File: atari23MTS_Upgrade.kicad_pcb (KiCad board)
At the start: 2 copper layers, 136 x 88 mm, 58 parts, among them P1 CONN_01X01, P2 CONN_01X01, P3 CONN_01X01, P4 CONN_01X01, P5 CONN_01X01, P6 CONN_01X01, SW1 SW_PUSH, U1 NCP1117ST33T3G, U10 TXB0108-PW, U11 ISSI61WV5128BL, U12 ISSI61WV5128BL, U13 ISSI61WV5128BL, U14 ISSI61WV5128BL, U2 STM32F401RCTx, U3 74LS138, U4 TXB0108-PW, U5 TXB0108-PW, U6 TXB0108-PW, U7 74HC04, U8 TXB0108-PW, U9 74LS32

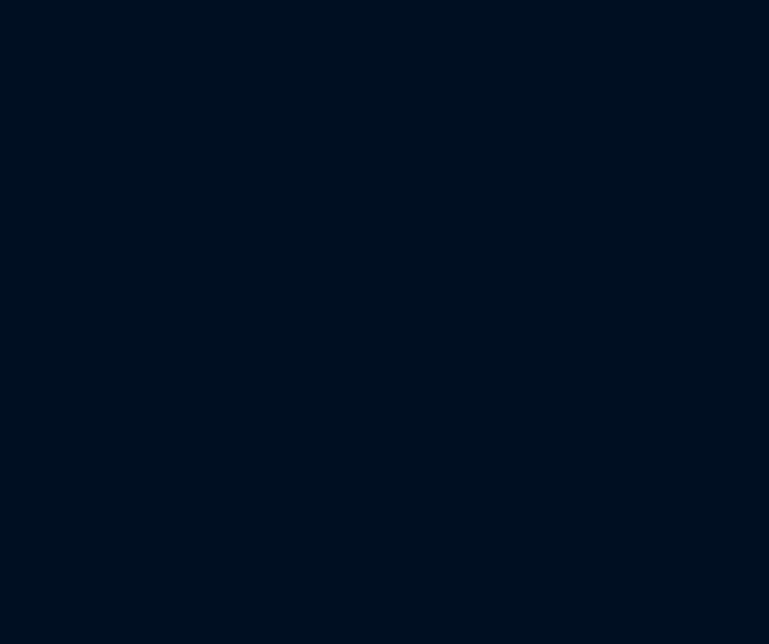
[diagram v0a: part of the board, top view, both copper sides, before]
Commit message: Modified silkscreen
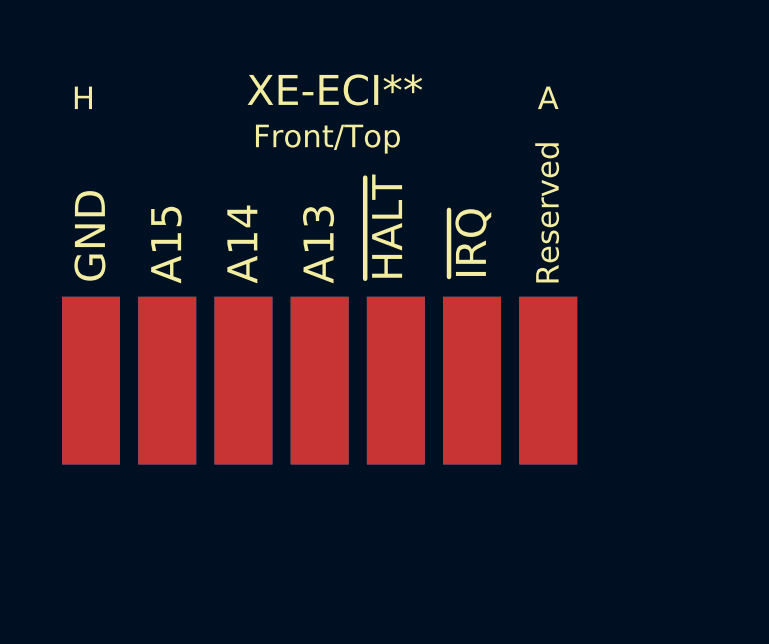
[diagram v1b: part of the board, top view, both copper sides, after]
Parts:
- removed LOGO: LOGO, RetroBitLab:atari_fuji_SilkScreen_21.2x25-RevBack
- added G***: LOGO, RetroBitLab:atari_fuji_SilkScreen_21.2x25-Rev, B.Cu at (152.4, 86.4)
- added XE-ECI**: ATARI-XE-ECI-SLOT, ATARI-XE-ECI-SLOT, F.Cu at (0.00, 0.00)

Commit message: Updated after footprint ECI Change
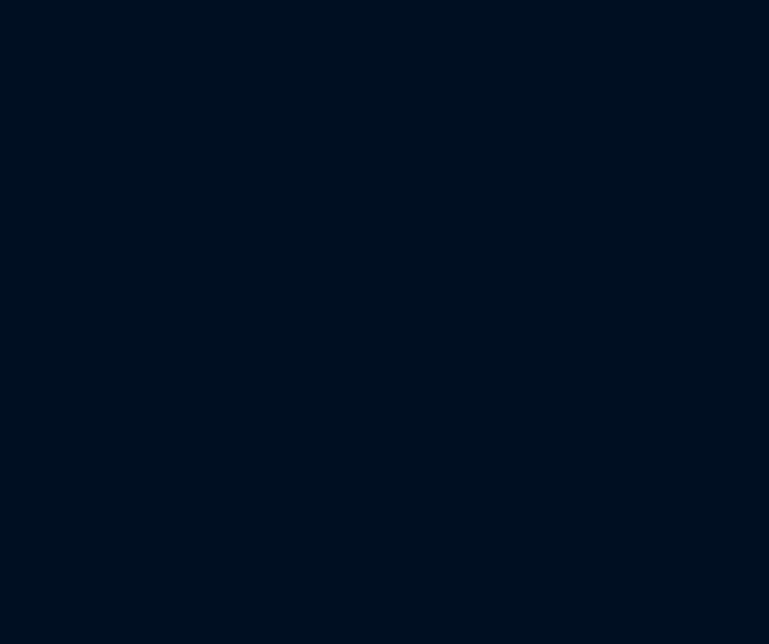
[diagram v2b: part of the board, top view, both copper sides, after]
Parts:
- removed XE-ECI**: ATARI-XE-ECI-SLOT, ATARI-XE-ECI-SLOT
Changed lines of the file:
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@@
 (kicad_pcb (version 4) (host pcbnew 4.0.2+dfsg1-stable)
   (general
-    (links 0)
+    (links 356)
     (no_connects 0)
-    (area 84.949999 50.449999 221.050001 138.550001)
+    (area -0.45 -14.587 243.5 161.200001)
     (thickness 1.6)
     (drawings 48)
     (tracks 2906)
     (zones 0)
-    (modules 59)
+    (modules 58)
     (nets 108)
   )
@@
     (uvia_drill 0.1)
   )
-  (module ATARI-XE-ECI-SLOT (layer F.Cu)
-    (at 0 0)
-    (fp_text reference XE-ECI** (at 10.16 -13.462) (layer F.SilkS)
-      (effects (font (size 1 1) (thickness 0.15)))
-    )
-    (fp_text value ATARI-XE-ECI-SLOT (at 9.652 -11.938) (layer F.Fab)
-      (effects (font (size 1 1) (thickness 0.15)))
-    )
-    (fp_text user 7 (at 1.778 -13.208) (layer B.SilkS)
-      (effects (font (size 0.75 0.75) (thickness 0.15)) (justify mirror))
-    )
-    (fp_text user 1 (at 17.272 -13.208) (layer B.SilkS)
-      (effects (font (size 0.75 0.75) (thickness 0.15)) (justify mirror))
-    )
-    (fp_text user Back/Bottom (at 9.652 -12.446) (layer B.SilkS)
-      (effects (font (size 0.75 0.75) (thickness 0.15)) (justify mirror))
-    )
-    (fp_text user Front/Top (at 9.906 -11.938) (layer F.SilkS)
-      (effects (font (size 0.75 0.75) (thickness 0.15)))
-    )
-    (fp_text user H (at 1.778 -13.208) (layer F.SilkS)
-      (effects (font (size 0.75 0.75) (thickness 0.15)))
-    )
-    (fp_text user A (at 17.272 -13.208) (layer F.SilkS)
-      (effects (font (size 0.75 0.75) (thickness 0.15)))
-    )
-    (fp_text user Reserved (at 17.272 -9.398 90) (layer F.SilkS)
-      (effects (font (size 0.75 0.75) (thickness 0.15)))
-    )
-    (fp_text user ~IRQ (at 14.732 -8.382 90) (layer F.SilkS)
-      (effects (font (size 1 1) (thickness 0.15)))
-    )
-    (fp_text user ~HALT (at 11.938 -8.89 90) (layer F.SilkS)
-      (effects (font (size 1 1) (thickness 0.15)))
-    )
-    (fp_text user A13 (at 9.652 -8.382 90) (layer F.SilkS)
-      (effects (font (size 1 1) (thickness 0.15)))
-    )
-    (fp_text user A14 (at 7.112 -8.382 90) (layer F.SilkS)
-      (effects (font (size 1 1) (thickness 0.15)))
-    )
-    (fp_text user A15 (at 4.572 -8.382 90) (layer F.SilkS)
-      (effects (font (size 1 1) (thickness 0.15)))
-    )
-    (fp_text user ~REF (at 4.572 -8.636 90) (layer B.SilkS)
-      (effects (font (size 1 1) (thickness 0.15)) (justify mirror))
-    )
-    (fp_text user AUDIO (at 7.112 -9.144 90) (layer B.SilkS)
-      (effects (font (size 1 1) (thickness 0.15)) (justify mirror))
-    )
-    (fp_text user ~MPD (at 9.652 -8.636 90) (layer B.SilkS)
-      (effects (font (size 1 1) (thickness 0.15)) (justify mirror))
-    )
-    (fp_text user ~D1XX (at 12.192 -8.89 90) (layer B.SilkS)
-      (effects (font (size 1 1) (thickness 0.15)) (justify mirror))
-    )
-    (fp_text user ~RST (at 14.732 -8.382 90) (layer B.SilkS)
-      (effects (font (size 1 1) (thickness 0.15)) (justify mirror))
-    )
-    (fp_text user ~EXSEL (at 17.272 -9.144 90) (layer B.SilkS)
-      (effects (font (size 1 1) (thickness 0.15)) (justify mirror))
-    )
-    (fp_text user 5V (at 2.032 -8.128 90) (layer B.SilkS)
-      (effects (font (size 1 1) (thickness 0.15)) (justify mirror))
-    )
-    (fp_text user GND (at 2.032 -8.636 90) (layer F.SilkS)
-      (effects (font (size 1 1) (thickness 0.15)))
-    )
-    (pad A smd rect (at 17.272 -3.81 270) (size 5.588 1.9304) (layers F.Cu F.Paste F.Mask))
-    (pad 1 smd rect (at 17.272 -3.81 270) (size 5.588 1.9304) (layers B.Cu B.Paste B.Mask))
-    (pad 2 smd rect (at 14.732 -3.81 270) (size 5.588 1.9304) (layers B.Cu B.Paste B.Mask))
-    (pad 3 smd rect (at 12.192 -3.81 270) (size 5.588 1.9304) (layers B.Cu B.Paste B.Mask))
-    (pad 4 smd rect (at 9.652 -3.81 270) (size 5.588 1.9304) (layers B.Cu B.Paste B.Mask))
-    (pad 5 smd rect (at 7.112 -3.81 270) (size 5.588 1.9304) (layers B.Cu B.Paste B.Mask))
-    (pad 6 smd rect (at 4.572 -3.81 270) (size 5.588 1.9304) (layers B.Cu B.Paste B.Mask))
-    (pad 7 smd rect (at 2.032 -3.81 270) (size 5.588 1.9304) (layers B.Cu B.Paste B.Mask))
-    (pad B smd rect (at 14.732 -3.81 270) (size 5.588 1.9304) (layers F.Cu F.Paste F.Mask))
-    (pad C smd rect (at 12.192 -3.81 270) (size 5.588 1.9304) (layers F.Cu F.Paste F.Mask))
-    (pad D smd rect (at 9.652 -3.81 270) (size 5.588 1.9304) (layers F.Cu F.Paste))
-    (pad E smd rect (at 7.112 -3.81 270) (size 5.588 1.9304) (layers F.Cu F.Paste F.Mask))
-    (pad F smd rect (at 4.572 -3.81 270) (size 5.588 1.9304) (layers F.Cu F.Paste F.Mask))
-    (pad H smd rect (at 2.032 -3.81 270) (size 5.588 1.9304) (layers F.Cu F.Paste F.Mask))
-  )
   (module ATARI-LEFT-CARTRIDGE locked (layer F.Cu)
     (at 148.082 126.238)
@@
     (pad C smd rect (at 12.192 -3.81 270) (size 5.588 1.9304) (layers F.Cu F.Paste F.Mask)
       (net 40 ~HALT))
-    (pad D smd rect (at 9.652 -3.81 270) (size 5.588 1.9304) (layers F.Cu F.Paste)
+    (pad D smd rect (at 9.652 -3.81 270) (size 5.588 1.9304) (layers F.Cu F.Paste F.Mask)
       (net 41 A13))
     (pad E smd rect (at 7.112 -3.81 270) (size 5.588 1.9304) (layers F.Cu F.Paste F.Mask)

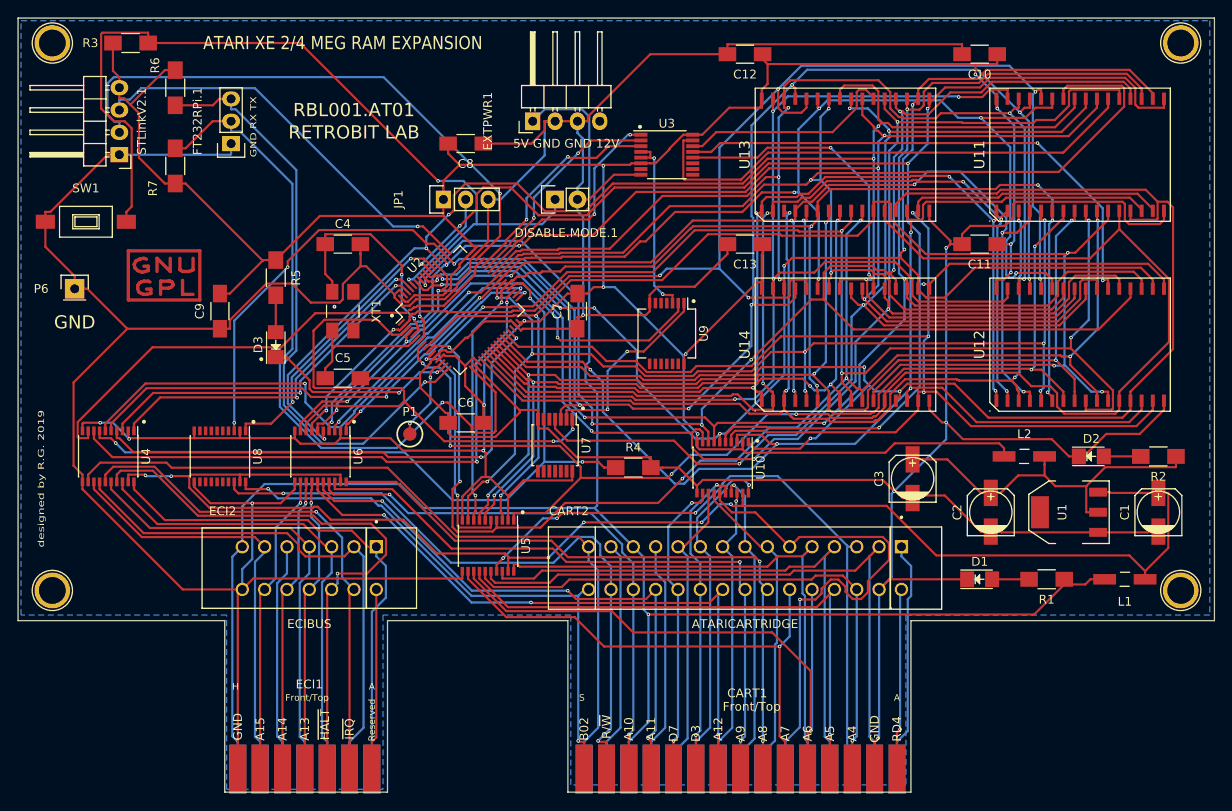
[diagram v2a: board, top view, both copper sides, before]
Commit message: Added D3xx selection logic for PIA (6520) if needed
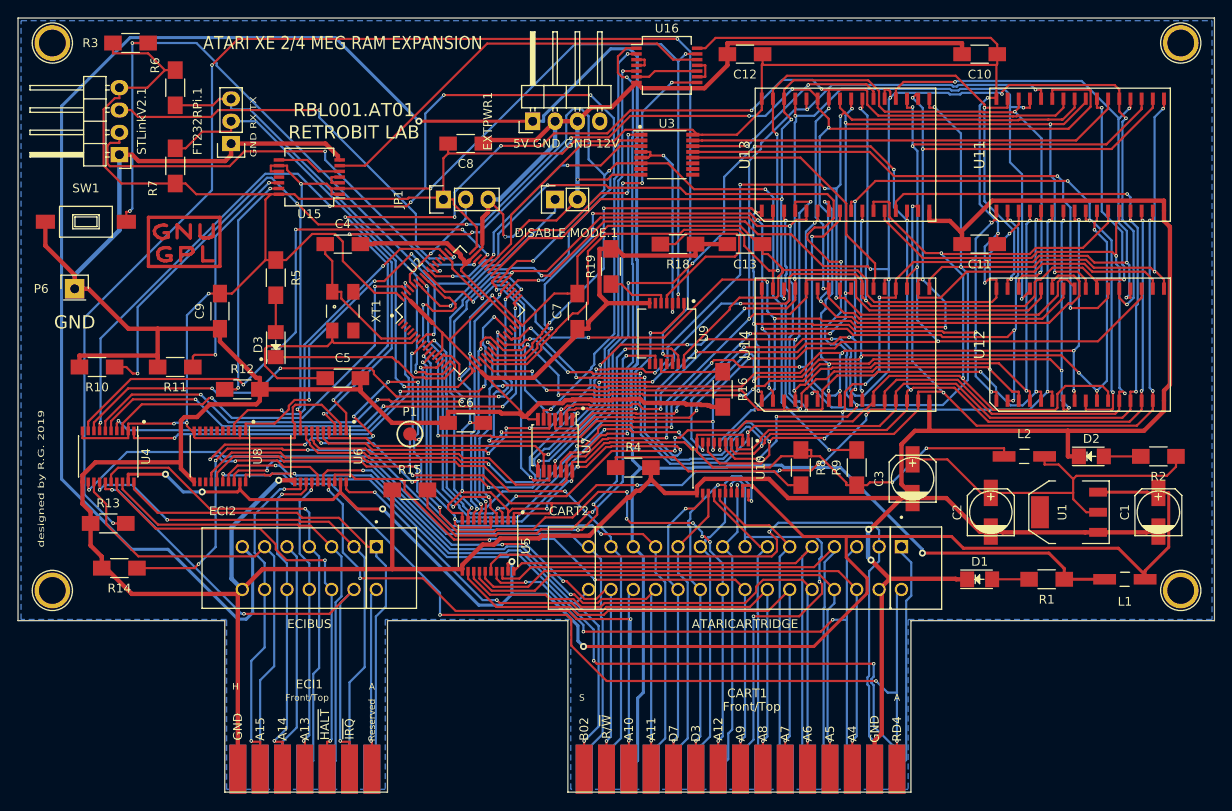
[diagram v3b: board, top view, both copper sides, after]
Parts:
- added R10: 2.2k, Resistors_SMD:R_1206_HandSoldering, F.Cu at (94.0, 90.2)
- added R11: 0, Resistors_SMD:R_1206_HandSoldering, F.Cu at (102.9, 90.2)
- added R12: 0, Resistors_SMD:R_1206_HandSoldering, F.Cu at (110.5, 92.7)
- added R13: 0, Resistors_SMD:R_1206_HandSoldering, F.Cu at (95.2, 108.0)
- added R14: 0, Resistors_SMD:R_1206_HandSoldering, F.Cu at (96.5, 113.0)
- added R15: 0, Resistors_SMD:R_1206_HandSoldering, F.Cu at (129.5, 104.1)
- added R16: 0, Resistors_SMD:R_1206_HandSoldering, F.Cu at (165.1, 92.7)
- added R18: 0, Resistors_SMD:R_1206_HandSoldering, F.Cu at (160.0, 76.2)
- added R19: 0, Resistors_SMD:R_1206_HandSoldering, F.Cu at (152.4, 78.7)
- added R8: 10K, Resistors_SMD:R_1206_HandSoldering, F.Cu at (174.0, 101.6)
- added R9: 10K, Resistors_SMD:R_1206_HandSoldering, F.Cu at (180.3, 101.6)
- added U15: 74LS08, Housings_SSOP:SSOP-14_5.3x6.2mm_Pitch0.65mm, F.Cu at (118.1, 68.6)
- added U16: 74LS08, Housings_SSOP:SSOP-14_5.3x6.2mm_Pitch0.65mm, F.Cu at (158.8, 55.9)
- moved REF** 4.44 mm to (103.9, 76.2)
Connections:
- EXTPWR1 pad 4: (no net) -> Net-(EXTPWR1-Pad4)
- P2 pad 1: (no net) -> Net-(P2-Pad1)
- P3 pad 1: (no net) -> Net-(P3-Pad1)
- P4 pad 1: (no net) -> Net-(P4-Pad1)
- P5 pad 1: (no net) -> Net-(P5-Pad1)
- R4 pad 1: ~mRST -> Net-(R4-Pad1)
- U2 pad 1: (no net) -> Net-(U2-Pad1)
- U2 pad 2: mA13 -> Net-(U2-Pad2)
- U2 pad 3: mA14 -> Net-(U2-Pad3)
- U2 pad 30: (no net) -> Net-(U2-Pad30)
- U2 pad 39: mA8 -> RAMEN
- U2 pad 4: mA15 -> Net-(U2-Pad4)
- U2 pad 40: mA9 -> ~mD3XX
- U2 pad 51: mA10 -> Net-(U2-Pad51)
- U2 pad 52: mA11 -> Net-(U2-Pad52)
- U2 pad 53: mA12 -> Net-(U2-Pad53)
- U3 pad 10: (no net) -> Net-(U3-Pad10)
- U3 pad 11: (no net) -> Net-(U3-Pad11)
- U3 pad 6: VCC3V3 -> RAMEN
- U3 pad 7: (no net) -> Net-(U3-Pad7)
- U3 pad 9: (no net) -> Net-(U3-Pad9)
- U7 pad 10: (no net) -> ~mD3XX
- U7 pad 11: (no net) -> mD3XX
- U7 pad 12: (no net) -> ~mA13
- U7 pad 13: (no net) -> mA13
- U7 pad 5: (no net) -> mA11
- U7 pad 6: (no net) -> ~mA11
- U7 pad 8: (no net) -> ~mA10
- U7 pad 9: (no net) -> mA10
- U8 pad 12: (no net) -> Net-(U8-Pad12)
- U8 pad 13: (no net) -> Net-(U8-Pad13)
- U8 pad 14: (no net) -> RD5
- U8 pad 15: (no net) -> ~S5
- U8 pad 16: (no net) -> RD4
- U8 pad 17: (no net) -> ~S4
- U8 pad 4: (no net) -> ~mS4
- U8 pad 5: (no net) -> mRD4
- U8 pad 6: (no net) -> ~mS5
- U8 pad 7: (no net) -> mRD5
- U8 pad 8: (no net) -> Net-(U8-Pad8)
- U8 pad 9: (no net) -> Net-(U8-Pad9)
- U9 pad 10: (no net) -> Net-(R16-Pad1)
- U9 pad 11: (no net) -> Net-(U9-Pad11)
- U9 pad 12: (no net) -> Net-(R13-Pad2)
- U9 pad 13: (no net) -> Net-(R14-Pad1)
- U9 pad 4: (no net) -> Net-(R18-Pad2)
- U9 pad 5: (no net) -> Net-(R19-Pad1)
- U9 pad 6: (no net) -> Net-(U9-Pad6)
- U9 pad 8: (no net) -> Net-(U9-Pad8)
- U9 pad 9: (no net) -> Net-(R15-Pad2)
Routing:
- net RAMEN: track 0.00 -> 158.5 mm, vias 0 -> 7
- net Net-(R13-Pad2): track 0.00 -> 154.8 mm, vias 0 -> 4
- net GND: track 629.2 -> 745.2 mm
- net VCC3V3: track 411.0 -> 526.5 mm, vias 13 -> 15
- net +5VDC: track 212.8 -> 315.5 mm, vias 1 -> 2
- net ~S4: track 26.4 -> 126.0 mm, vias 0 -> 3
- net Net-(R14-Pad1): track 0.00 -> 96.1 mm, vias 0 -> 6
- net RD4: track 20.6 -> 111.8 mm, vias 1 -> 4
- net mA15: track 58.1 -> 116.9 mm, vias 3 -> 5
- net ~S5: track 26.4 -> 83.9 mm, vias 0 -> 2
- net ~mA13: track 0.00 -> 56.7 mm, vias 0 -> 2
- net mD3XX: track 0.00 -> 53.8 mm, vias 0 -> 4
- net A12: track 73.6 -> 126.9 mm, vias 3 -> 14
- net RD5: track 26.4 -> 78.9 mm, vias 0 -> 1
- net ~mA10: track 0.00 -> 51.7 mm, vias 0 -> 2
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
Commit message: Modified for GND & VCC track size
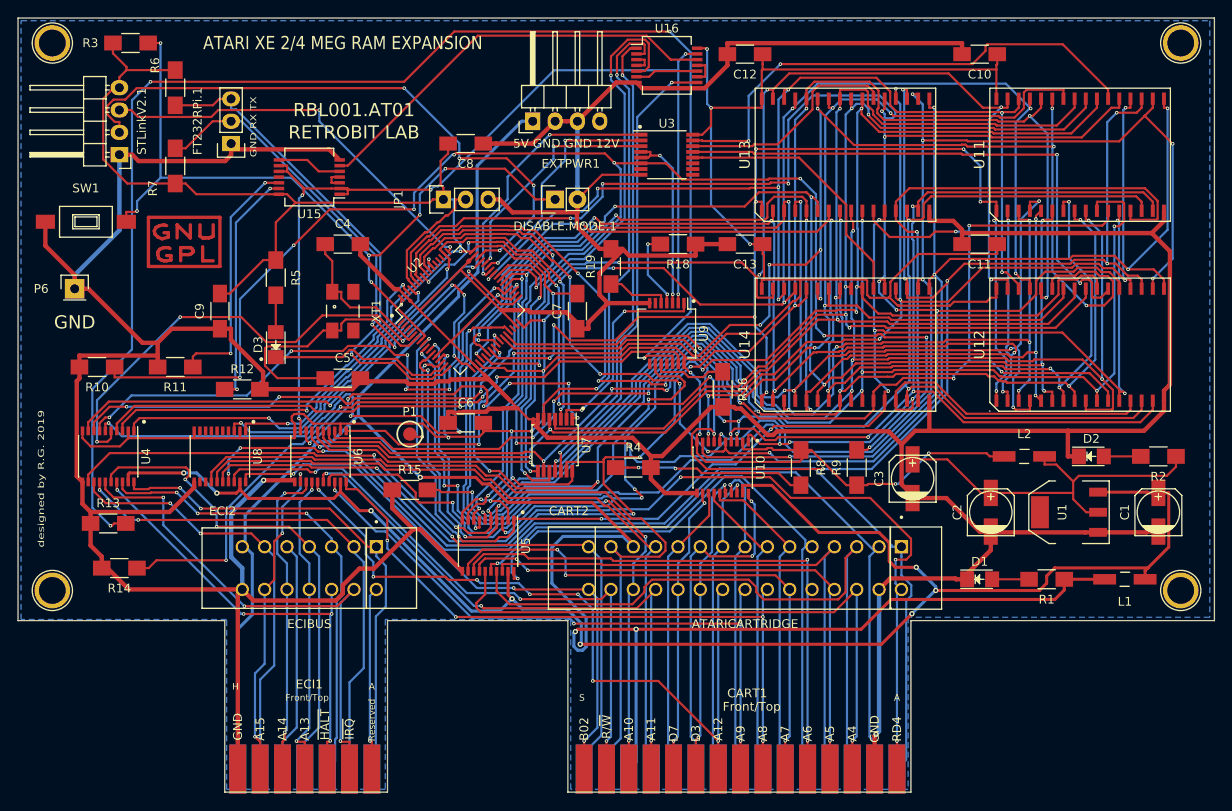
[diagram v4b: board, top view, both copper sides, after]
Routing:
- net +5VDC: track 315.5 -> 234.2 mm, vias 2 -> 3
- net VCC3V3: track 526.5 -> 466.9 mm, vias 15 -> 19
- net GND: track 745.2 -> 691.0 mm, vias 6 -> 2
- net mD1: track 190.8 -> 139.9 mm, vias 11 -> 6
- net ~mRST: track 115.5 -> 64.8 mm
- net A12: track 126.9 -> 85.8 mm, vias 14 -> 7
- net mD0: track 145.4 -> 183.2 mm, vias 7 -> 5
- net mD3: track 202.5 -> 170.7 mm, vias 10 -> 9
- net mA1: track 158.9 -> 186.7 mm, vias 7 -> 11
- net mA8: track 191.0 -> 164.4 mm, vias 8 -> 10
- net mD6: track 194.2 -> 168.4 mm, vias 12 -> 10
- net mA4: track 143.7 -> 163.5 mm
- net Net-(R14-Pad1): track 96.1 -> 76.7 mm, vias 6 -> 4
- net mA9: track 179.3 -> 161.9 mm
- net PB0: track 113.5 -> 130.5 mm, vias 6 -> 8
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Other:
- net class +5VDC added: clearance 0.2, trace_width 0.35, via_dia 0.6, via_drill 0.3
- net class GND: via_dia 0.8 -> 0.6; via_drill 0.4 -> 0.3
- net class VCC5V: via_dia 0.8 -> 0.6; via_drill 0.4 -> 0.3
